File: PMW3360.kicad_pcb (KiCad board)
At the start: 2 copper layers, 39.8 x 15.1 mm, 10 parts, among them J1 Conn_01x07, U1 PMW3360, U2 TCR2EF19

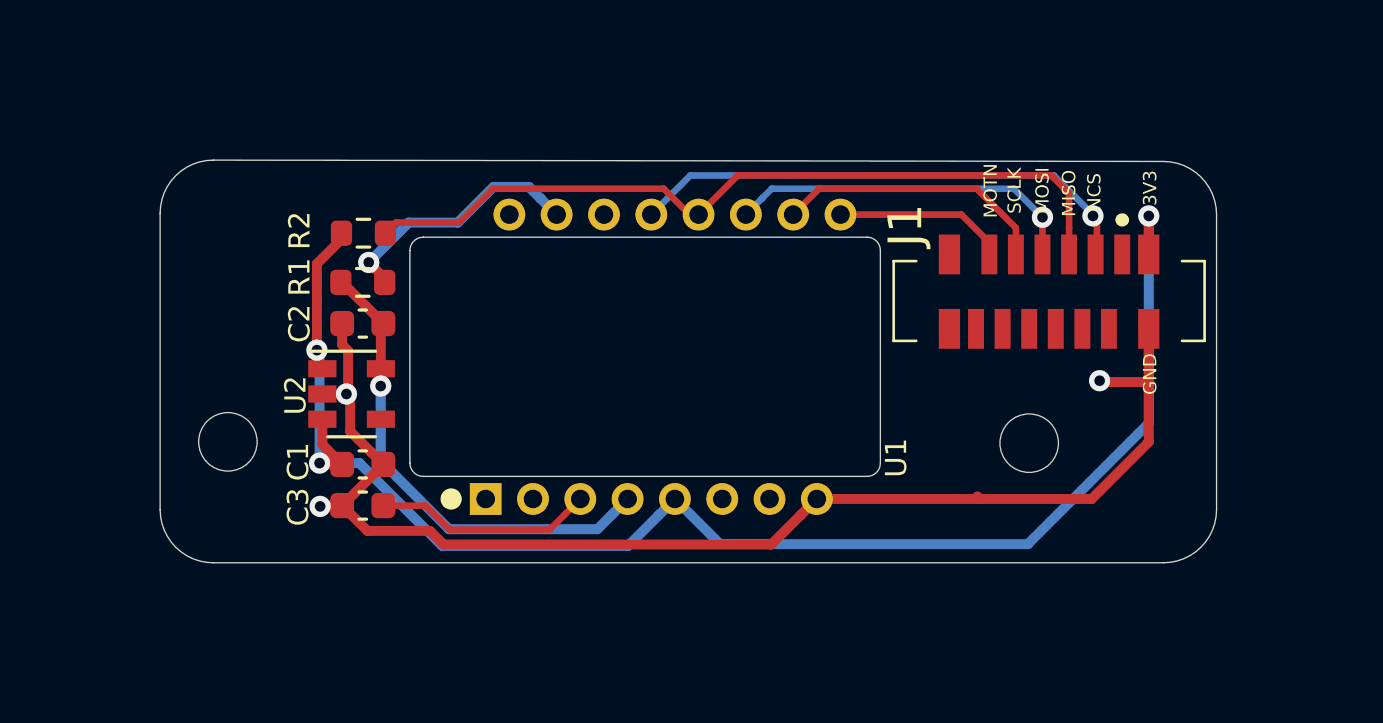
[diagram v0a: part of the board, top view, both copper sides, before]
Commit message: Adjusted board edges so it is square and the main measures are rounded.
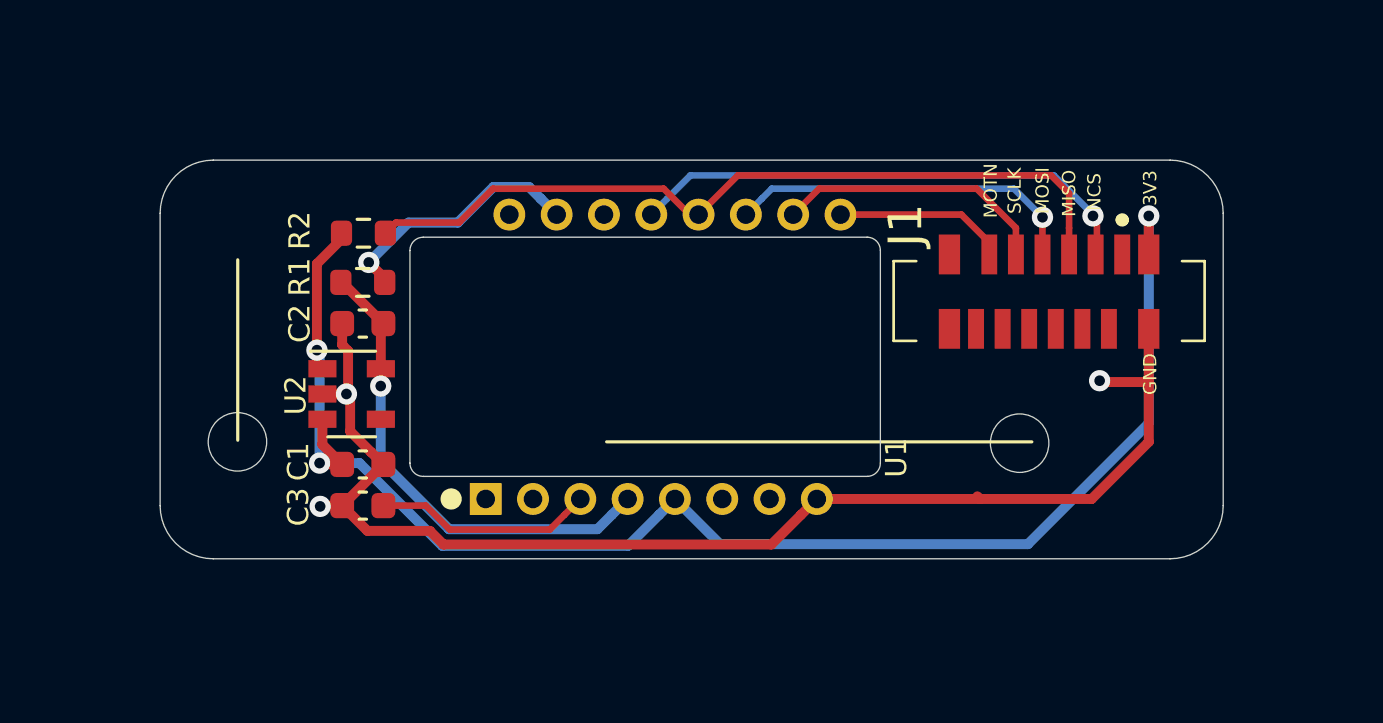
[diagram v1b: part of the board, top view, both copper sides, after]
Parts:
- moved H2 0.36 mm to (144.1, 108.0)
- moved H1 0.36 mm to (173.5, 108.1)
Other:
- board size 39.8 x 15.1 mm -> 40 x 15 mm
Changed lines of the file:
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@@
   (general
     (thickness 1.6)
-    (drawings 28)
+    (drawings 33)
     (tracks 111)
     (zones 0)
@@
     (46 B.CrtYd user)
     (47 F.CrtYd user)
-    (48 B.Fab user hide)
-    (49 F.Fab user hide)
+    (48 B.Fab user)
+    (49 F.Fab user)
   )
   (setup
@@
   )
   (module MountingHole:MountingHole_2.2mm_M2 locked (layer F.Cu)
-    (at 143.7 108.05)
+    (at 144.06 108.05)
     (descr "Mounting Hole 2.2mm, no annular, M2")
     (tags "mounting hole 2.2mm no annular m2")
@@
   )
   (module MountingHole:MountingHole_2.2mm_M2 locked (layer F.Cu)
-    (at 173.85 108.1)
+    (at 173.49 108.1)
     (descr "Mounting Hole 2.2mm, no annular, M2")
     (tags "mounting hole 2.2mm no annular m2")
@@
     (pad 1 smd rect (at -2.75 1.4 180) (size 0.6 1.5) (layers F.Cu F.Paste F.Mask))
   )
-  (module PMW3360:PMW3360 (layer F.Cu)
+  (module PMW3360:PMW3360 locked (layer F.Cu)
     (at 153.4 110.2 90)
     (fp_text reference U1 (at 1.55 15.45 90) (layer F.SilkS)
@@
     )
   )
+  (dimension 3.2 (width 0.12) (layer F.SilkS)
+    (gr_text "3.200 mm" (at 154.75 106.46 270) (layer F.SilkS)
+      (effects (font (size 1 1) (thickness 0.15)))
+    )
+    (feature1 (pts (xy 159.04 108.06) (xy 155.433579 108.06)))
+    (feature2 (pts (xy 159.04 104.86) (xy 155.433579 104.86)))
+    (crossbar (pts (xy 156.02 104.86) (xy 156.02 108.06)))
+    (arrow1a (pts (xy 156.02 108.06) (xy 155.433579 106.933496)))
+    (arrow1b (pts (xy 156.02 108.06) (xy 156.606421 106.933496)))
+    (arrow2a (pts (xy 156.02 104.86) (xy 155.433579 105.986504)))
+    (arrow2b (pts (xy 156.02 104.86) (xy 156.606421 105.986504)))
+  )
+  (gr_line (start 173.95 108.05) (end 157.95 108.05) (layer F.SilkS) (width 0.12))
+  (dimension 15.000003 (width 0.12) (layer F.SilkS)
+    (gr_text "15.000 mm" (at 151.576537 95.030201 -0.03819718068) (layer F.SilkS)
+      (effects (font (size 1 1) (thickness 0.15)))
+    )
+    (feature1 (pts (xy 144.07 104.83) (xy 144.076081 95.70878)))
+    (feature2 (pts (xy 159.07 104.84) (xy 159.076081 95.71878)))
+    (crossbar (pts (xy 159.07569 96.305201) (xy 144.07569 96.295201)))
+    (arrow1a (pts (xy 144.07569 96.295201) (xy 145.202584 95.709531)))
+    (arrow1b (pts (xy 144.07569 96.295201) (xy 145.201803 96.882373)))
+    (arrow2a (pts (xy 159.07569 96.305201) (xy 157.949577 95.718029)))
+    (arrow2b (pts (xy 159.07569 96.305201) (xy 157.948796 96.890871)))
+  )
+  (gr_line (start 144.07 107.99) (end 144.07 101.2) (layer F.SilkS) (width 0.12))
+  (dimension 17.890003 (width 0.12) (layer F.SilkS)
+    (gr_text "17.890 mm" (at 150.108304 92.876508 0.03202670405) (layer F.SilkS)
+      (effects (font (size 1 1) (thickness 0.15)))
+    )
+    (feature1 (pts (xy 141.17 104.86) (xy 141.163686 93.565087)))
+    (feature2 (pts (xy 159.06 104.85) (xy 159.053686 93.555087)))
+    (crossbar (pts (xy 159.054014 94.141508) (xy 141.164014 94.151508)))
+    (arrow1a (pts (xy 141.164014 94.151508) (xy 142.29019 93.564458)))
+    (arrow1b (pts (xy 141.164014 94.151508) (xy 142.290845 94.737299)))
+    (arrow2a (pts (xy 159.054014 94.141508) (xy 157.927183 93.555717)))
+    (arrow2b (pts (xy 159.054014 94.141508) (xy 157.927838 94.728558)))
+  )
+  (dimension 40 (width 0.12) (layer F.SilkS)
+    (gr_text "40.000 mm" (at 161.15 90.18) (layer F.SilkS)
+      (effects (font (size 1 1) (thickness 0.15)))
+    )
+    (feature1 (pts (xy 181.15 99.45) (xy 181.15 90.863579)))
+    (feature2 (pts (xy 141.15 99.45) (xy 141.15 90.863579)))
+    (crossbar (pts (xy 141.15 91.45) (xy 181.15 91.45)))
+    (arrow1a (pts (xy 181.15 91.45) (xy 180.023496 92.036421)))
+    (arrow1b (pts (xy 181.15 91.45) (xy 180.023496 90.863579)))
+    (arrow2a (pts (xy 141.15 91.45) (xy 142.276504 92.036421)))
+    (arrow2b (pts (xy 141.15 91.45) (xy 142.276504 90.863579)))
+  )
+  (dimension 15 (width 0.12) (layer F.SilkS)
+    (gr_text "15.000 mm" (at 185.919996 104.95 270) (layer F.SilkS)
+      (effects (font (size 1 1) (thickness 0.15)))
+    )
+    (feature1 (pts (xy 179.15 112.45) (xy 185.236417 112.45)))
+    (feature2 (pts (xy 179.15 97.45) (xy 185.236417 97.45)))
+    (crossbar (pts (xy 184.649996 97.45) (xy 184.649996 112.45)))
+    (arrow1a (pts (xy 184.649996 112.45) (xy 184.063575 111.323496)))
+    (arrow1b (pts (xy 184.649996 112.45) (xy 185.236417 111.323496)))
+    (arrow2a (pts (xy 184.649996 97.45) (xy 184.063575 98.576504)))
+    (arrow2b (pts (xy 184.649996 97.45) (xy 185.236417 98.576504)))
+  )
   (gr_text PMW3360 (at 174.75 103.25 180) (layer B.SilkS)
     (effects (font (size 2 1.5) (thickness 0.3)) (justify mirror))
@@
     (effects (font (size 2 1.5) (thickness 0.3)) (justify mirror))
   )
-  (dimension 22 (width 0.15) (layer Cmts.User)
-    (gr_text "22,000 mm" (at 186.65 104.65 90) (layer Cmts.User)
-      (effects (font (size 1 1) (thickness 0.15)))
-    )
-    (feature1 (pts (xy 183.35 93.65) (xy 185.936421 93.65)))
-    (feature2 (pts (xy 183.35 115.65) (xy 185.936421 115.65)))
-    (crossbar (pts (xy 185.35 115.65) (xy 185.35 93.65)))
-    (arrow1a (pts (xy 185.35 93.65) (xy 185.936421 94.776504)))
-    (arrow1b (pts (xy 185.35 93.65) (xy 184.763579 94.776504)))
-    (arrow2a (pts (xy 185.35 115.65) (xy 185.936421 114.523496)))
-    (arrow2b (pts (xy 185.35 115.65) (xy 184.763579 114.523496)))
-  )
-  (dimension 34 (width 0.15) (layer Cmts.User)
-    (gr_text "34,000 mm" (at 156.15 90.55) (layer Cmts.User)
-      (effects (font (size 1 1) (thickness 0.15)))
-    )
-    (feature1 (pts (xy 173.15 93.85) (xy 173.15 91.263579)))
-    (feature2 (pts (xy 139.15 93.85) (xy 139.15 91.263579)))
-    (crossbar (pts (xy 139.15 91.85) (xy 173.15 91.85)))
-    (arrow1a (pts (xy 173.15 91.85) (xy 172.023496 92.436421)))
-    (arrow1b (pts (xy 173.15 91.85) (xy 172.023496 91.263579)))
-    (arrow2a (pts (xy 139.15 91.85) (xy 140.276504 92.436421)))
-    (arrow2b (pts (xy 139.15 91.85) (xy 140.276504 91.263579)))
-  )
   (gr_text NCS (at 176.3 98.65 90) (layer F.SilkS)
     (effects (font (size 0.5 0.5) (thickness 0.1)))
@@
     (effects (font (size 0.5 0.5) (thickness 0.1)))
   )
-  (gr_arc (start 178.9 110.6) (end 178.9 112.6) (angle -90) (layer Edge.Cuts) (width 0.05))
-  (gr_arc (start 178.9 99.5) (end 180.9 99.5) (angle -90) (layer Edge.Cuts) (width 0.05))
-  (gr_arc (start 143.15 110.6) (end 141.15 110.6) (angle -90) (layer Edge.Cuts) (width 0.05))
+  (gr_arc (start 179.15 110.45) (end 179.15 112.45) (angle -90) (layer Edge.Cuts) (width 0.05))
+  (gr_arc (start 179.15 99.45) (end 181.15 99.45) (angle -90) (layer Edge.Cuts) (width 0.05))
+  (gr_arc (start 143.15 110.45) (end 141.15 110.45) (angle -90) (layer Edge.Cuts) (width 0.05))
   (gr_arc (start 143.15 99.45) (end 143.15 97.45) (angle -90) (layer Edge.Cuts) (width 0.05))
   (gr_line (start 168.25 100.85) (end 168.25 108.85) (layer Edge.Cuts) (width 0.05))
@@
   (gr_arc (start 151.05 100.85) (end 151.05 100.35) (angle -90) (layer Edge.Cuts) (width 0.05))
   (gr_arc (start 151.05 108.85) (end 150.55 108.85) (angle -90) (layer Edge.Cuts) (width 0.05))
-  (gr_line (start 178.9 112.6) (end 143.15 112.6) (layer Edge.Cuts) (width 0.05))
-  (gr_line (start 180.9 99.5) (end 180.9 110.6) (layer Edge.Cuts) (width 0.05))
-  (gr_line (start 143.15 97.45) (end 178.9 97.5) (layer Edge.Cuts) (width 0.05))
-  (gr_line (start 141.15 110.6) (end 141.15 99.45) (layer Edge.Cuts) (width 0.05))
+  (gr_line (start 179.15 112.45) (end 143.15 112.45) (layer Edge.Cuts) (width 0.05))
+  (gr_line (start 181.15 99.45) (end 181.15 110.45) (layer Edge.Cuts) (width 0.05))
+  (gr_line (start 143.15 97.45) (end 179.15 97.45) (layer Edge.Cuts) (width 0.05))
+  (gr_line (start 141.15 110.45) (end 141.15 99.45) (layer Edge.Cuts) (width 0.05))
   (segment (start 147.255 108.155) (end 148 108.9) (width 0.375) (layer F.Cu) (net 1))
   (segment (start 147.255 107.2) (end 147.255 108.155) (width 0.375) (layer F.Cu) (net 1))
